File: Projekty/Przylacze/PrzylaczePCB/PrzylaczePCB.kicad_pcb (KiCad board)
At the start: 2 copper layers, 134.6 x 126 mm, 131 parts, among them J1 Conn_02x20_Odd_Even, J2 USB_B, J3 Conn_01x06, J4 Conn_02x04_Odd_Even, J5 Screw_Terminal_01x06, M3 MountingHole_3.2mm_M3, Q1 BC547, Q10 BC557, Q11 2N3904, Q12 2N7002, Q2 BC547, Q3 BC547, Q4 BC557, Q5 2N3904, Q6 BC557, Q7 BC557, Q8 BC547, Q9 BC557, SW1 SW_Push, SW2 SW_SPDT, SW3 SW_SPDT, SW4 SW_SPDT, SW5 SW_SPDT, SW6 SW_SPDT, SW7 SW_SPDT, SW8 SW_SPDT, SW9 SW_SPDT, U1 MCP2561-E-P, U2 ATSAM4S2AA-AU, U3 MCP2515-xSO, U4 TJA1055T_3_C,518, U5 MAX3485, U6 74AHC1G04, U7 LDL1117S33R, U8 DI78M05UAB, U9 74AHC1G04, Y1 20MHz

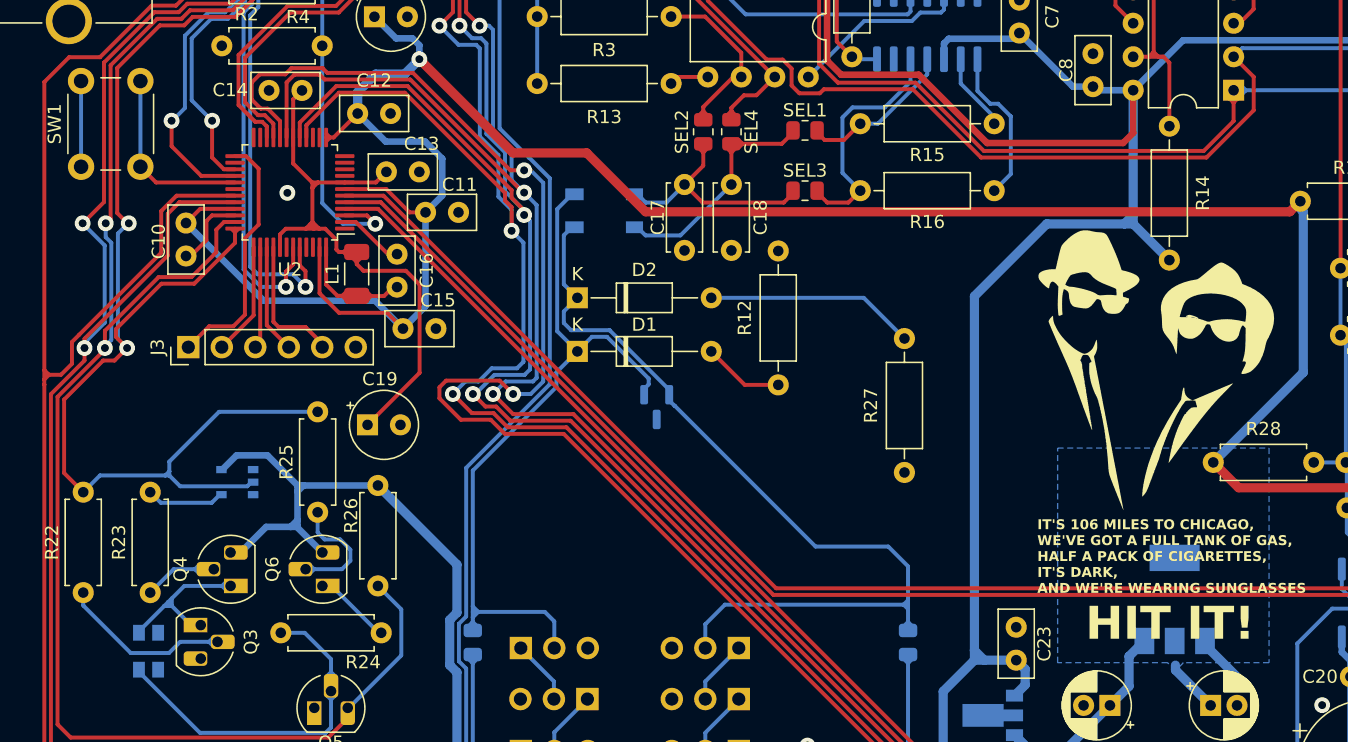
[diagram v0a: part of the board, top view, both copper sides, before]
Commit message: Przyłącze - projekt PCB v1.3.1
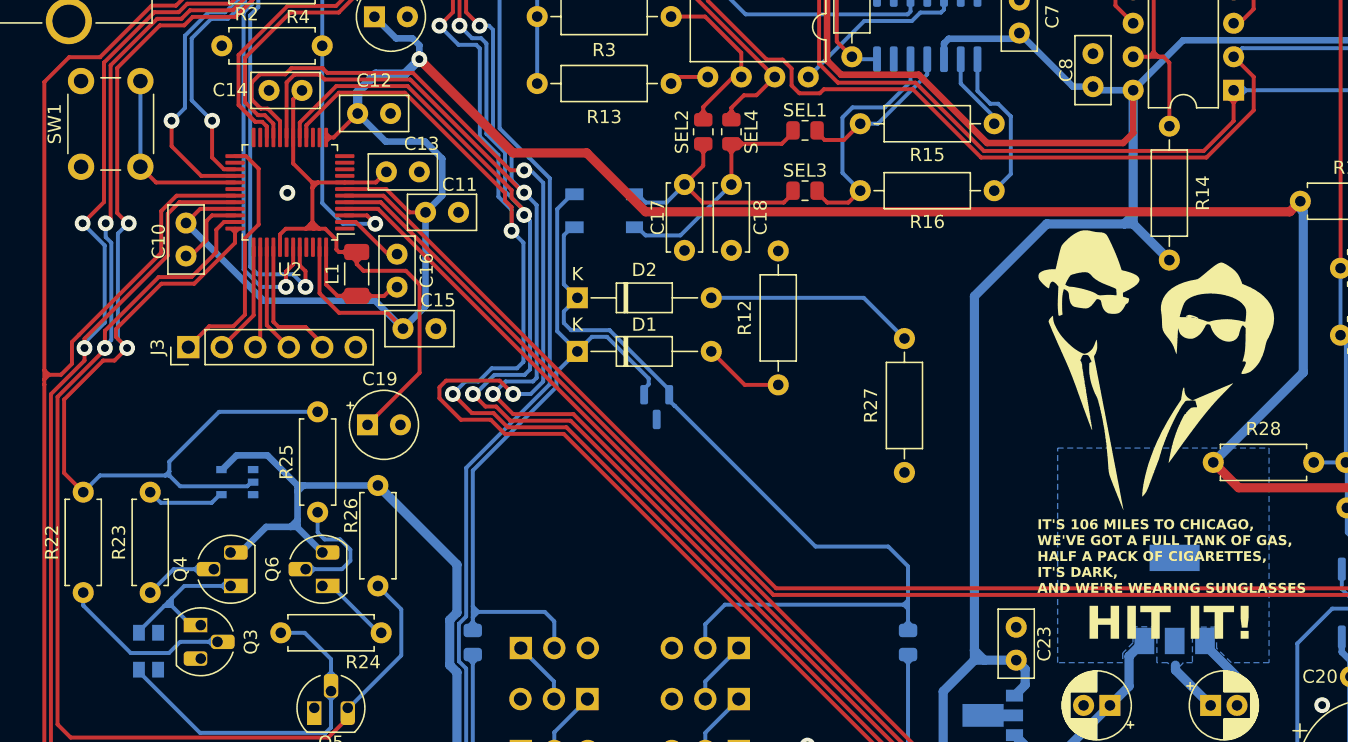
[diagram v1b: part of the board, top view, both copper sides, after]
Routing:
- net GND: track 20.7 -> 14.2 mm
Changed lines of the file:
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@@
   (via (at 102.59 166.37) (size 1.2) (drill 0.6) (layers "F.Cu" "B.Cu") (free) (net 1))
   (segment (start 132.751 158.731) (end 135.37 161.35) (width 0.7) (layer "B.Cu") (net 1))
-  (segment (start 47.49 115.96) (end 47.49 122.46) (width 0.3) (layer "B.Cu") (net 1))
   (segment (start 139.183068 125.876999) (end 139.983067 125.077) (width 0.7) (layer "F.Cu") (net 2))
   (segment (start 73.152 114.3) (end 80.264 121.412) (width 0.7) (layer "F.Cu") (net 2))
@@
         (xy 137.61 143.8)
         (xy 137.61 160.08)
+        (xy 134.75 160.08)
+        (xy 133.63 158.99)
+        (xy 133.62 157.38)
+        (xy 131.8 157.38)
+        (xy 131.8 160.08)
         (xy 131.11 160.08)
         (xy 130.51 160.7)
         (xy 129.91 160.08)
+        (xy 129.1 160.08)
+        (xy 129.1 157.36)
+        (xy 127.29 157.36)
+        (xy 127.29 158.57)
+        (xy 126.51 159.35)
+        (xy 126.51 160.08)
         (xy 121.57 160.08)
       )

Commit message: Przyłącze - projekt PCB v1.4
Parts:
- Q1, Q10, Q11, Q2, Q3, Q4, Q5, Q6, Q7, Q8, Q9: footprint Package_TO_SOT_THT:TO-92L_HandSolder -> Package_TO_SOT_THT:TO-92L
- moved C7 4.49 mm to (119.6, 114.2)
- moved R11 1.39 mm to (165.6, 93.8)
- moved C8 0.32 mm to (124.3, 114.2)
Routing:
- net Net-(Q6-B): track 9.96 -> 6.95 mm
- net +5V: track 318.7 -> 321.7 mm
- net +12V: track 106.1 -> 103.7 mm
- net Net-(Q10-B): track 9.14 -> 6.77 mm
- net Net-(D10-A): track 28.3 -> 26.1 mm
- net Net-(Q1-B): track 25.2 -> 23.1 mm
- net USBMON: track 23.8 -> 25.9 mm
- net Net-(U2-VDDPLL): track 10.0 -> 8.18 mm
- net Net-(D4-A): track 2.92 -> 4.74 mm
- net Net-(Q10-C): track 5.03 -> 6.59 mm
- net Net-(Q6-C): track 5.03 -> 6.50 mm
- net CANH: track 269.3 -> 267.9 mm
- net Net-(U2-VDDOUT): track 47.0 -> 45.8 mm
- net Net-(J2-D+): track 7.88 -> 6.81 mm
- net ERR: track 102.3 -> 103.3 mm
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- added copper zone on B.Cu, net +5V
- added copper zone on B.Cu, net Net-(U4-BAT)
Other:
- board text added: "Przyłącze stanowiskowe v1.4 Projekt kompetencyjny 2023 6EiT Grupa 7 - Sieci przemysłowe Maciej Kaczorowski, Maciej Mierzejek, Artur Poteraj, Rafał Skwirus Politechnika Łódzka WEEIA github.com/BlackHabanero/PKgr7Sieci"
- board text removed: "Przyłącze stanowiskowe v1.3 Projekt kompetencyjny 2023 6EiT Grupa 7 - Sieci przemysłowe Maciej Kaczorowski, Maciej Mierzejek, Artur Poteraj, Rafał Skwirus Politechnika Łódzka WEEIA github.com/BlackHabanero/PKgr7Sieci"

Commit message: Przyłącze - projekt PCB v1.4.1
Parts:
- J4: footprint Connector_PinHeader_2.54mm:PinHeader_2x04_P2.54mm_Vertical -> Connector_PinSocket_2.54mm:PinSocket_2x04_P2.54mm_Vertical; moved to B.Cu
- turned J4 to 180 degrees
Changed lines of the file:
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@@
     )
   )
-  (footprint "Connector_PinHeader_2.54mm:PinHeader_2x04_P2.54mm_Vertical" placed (layer "F.Cu")
-    (at 165.1 161.544)
-    (descr "Through hole straight pin header, 2x04, 2.54mm pitch, double rows")
-    (tags "Through hole pin header THT 2x04 2.54mm double row")
-    (property "Sheetfile" "PrzylaczePCB.kicad_sch")
-    (property "Sheetname" "")
-    (property "ki_description" "Generic connector, double row, 02x04, odd/even pin numbering scheme (row 1 odd numbers, row 2 even numbers), script generated (kicad-library-utils/schlib/autogen/connector/)")
-    (property "ki_keywords" "connector")
-    (attr through_hole)
-    (fp_text reference "J4" (at 1.27 -2.33) (layer "F.SilkS")
-        (effects (font (size 1 1) (thickness 0.15)))
-    )
-    (fp_text value "Conn_02x04_Odd_Even" (at 1.27 9.95) (layer "F.Fab")
-        (effects (font (size 1 1) (thickness 0.15)))
-    )
-    (fp_text user "${REFERENCE}" (at 1.27 3.81 90) (layer "F.Fab")
-        (effects (font (size 1 1) (thickness 0.15)))
-    )
-    (fp_line (start -1.33 -1.33) (end 0 -1.33)
-      (stroke (width 0.12) (type solid)) (layer "F.SilkS"))
-    (fp_line (start -1.33 0) (end -1.33 -1.33)
-      (stroke (width 0.12) (type solid)) (layer "F.SilkS"))
-    (fp_line (start -1.33 1.27) (end -1.33 8.95)
-      (stroke (width 0.12) (type solid)) (layer "F.SilkS"))
-    (fp_line (start -1.33 1.27) (end 1.27 1.27)
-      (stroke (width 0.12) (type solid)) (layer "F.SilkS"))
-    (fp_line (start -1.33 8.95) (end 3.87 8.95)
-      (stroke (width 0.12) (type solid)) (layer "F.SilkS"))
-    (fp_line (start 1.27 -1.33) (end 3.87 -1.33)
-      (stroke (width 0.12) (type solid)) (layer "F.SilkS"))
-    (fp_line (start 1.27 1.27) (end 1.27 -1.33)
-      (stroke (width 0.12) (type solid)) (layer "F.SilkS"))
-    (fp_line (start 3.87 -1.33) (end 3.87 8.95)
-      (stroke (width 0.12) (type solid)) (layer "F.SilkS"))
-    (fp_line (start -1.8 -1.8) (end -1.8 9.4)
-      (stroke (width 0.05) (type solid)) (layer "F.CrtYd"))
-    (fp_line (start -1.8 9.4) (end 4.35 9.4)
-      (stroke (width 0.05) (type solid)) (layer "F.CrtYd"))
-    (fp_line (start 4.35 -1.8) (end -1.8 -1.8)
-      (stroke (width 0.05) (type solid)) (layer "F.CrtYd"))
-    (fp_line (start 4.35 9.4) (end 4.35 -1.8)
-      (stroke (width 0.05) (type solid)) (layer "F.CrtYd"))
-    (fp_line (start -1.27 0) (end 0 -1.27)
-      (stroke (width 0.1) (type solid)) (layer "F.Fab"))
-    (fp_line (start -1.27 8.89) (end -1.27 0)
-      (stroke (width 0.1) (type solid)) (layer "F.Fab"))
-    (fp_line (start 0 -1.27) (end 3.81 -1.27)
-      (stroke (width 0.1) (type solid)) (layer "F.Fab"))
-    (fp_line (start 3.81 -1.27) (end 3.81 8.89)
-      (stroke (width 0.1) (type solid)) (layer "F.Fab"))
-    (fp_line (start 3.81 8.89) (end -1.27 8.89)
-      (stroke (width 0.1) (type solid)) (layer "F.Fab"))
-    (pad "1" thru_hole rect (at 0 0) (size 1.7 1.7) (drill 1) (layers "*.Cu" "*.Mask")
-      (net 1 "GND") (pinfunction "Pin_1") (pintype "passive"))
-    (pad "2" thru_hole oval (at 2.54 0) (size 1.7 1.7) (drill 1) (layers "*.Cu" "*.Mask")
-      (net 2 "+3.3V") (pinfunction "Pin_2") (pintype "passive"))
-    (pad "3" thru_hole oval (at 0 2.54) (size 1.7 1.7) (drill 1) (layers "*.Cu" "*.Mask")
-      (net 31 "CS0") (pinfunction "Pin_3") (pintype "passive"))
-    (pad "4" thru_hole oval (at 2.54 2.54) (size 1.7 1.7) (drill 1) (layers "*.Cu" "*.Mask")
-      (net 2 "+3.3V") (pinfunction "Pin_4") (pintype "passive"))
-    (pad "5" thru_hole oval (at 0 5.08) (size 1.7 1.7) (drill 1) (layers "*.Cu" "*.Mask")
-      (net 32 "SPCK") (pinfunction "Pin_5") (pintype "passive"))
-    (pad "6" thru_hole oval (at 2.54 5.08) (size 1.7 1.7) (drill 1) (layers "*.Cu" "*.Mask")
-      (net 33 "MOSI") (pinfunction "Pin_6") (pintype "passive"))
-    (pad "7" thru_hole oval (at 0 7.62) (size 1.7 1.7) (drill 1) (layers "*.Cu" "*.Mask")
-      (net 34 "MISO") (pinfunction "Pin_7") (pintype "passive"))
-    (pad "8" thru_hole oval (at 2.54 7.62) (size 1.7 1.7) (drill 1) (layers "*.Cu" "*.Mask")
-      (net 35 "RADIO_IRQ") (pinfunction "Pin_8") (pintype "passive"))
-    (model "${KICAD6_3DMODEL_DIR}/Connector_PinHeader_2.54mm.3dshapes/PinHeader_2x04_P2.54mm_Vertical.wrl"
-      (offset (xyz 0 0 0))
-      (scale (xyz 1 1 1))
-      (rotate (xyz 0 0 0))
-    )
-  )
   (footprint "Resistor_THT:R_Axial_DIN0207_L6.3mm_D2.5mm_P10.16mm_Horizontal" placed (layer "F.Cu")
     (at 105.966 103.955 -90)
@@
       (rotate (xyz 0 0 0))
     )
+    (model "${KIPRJMOD}/3DModels/USB-B-S-F-B-TH.stp"
+      (offset (xyz 7 -1.25 0))
+      (scale (xyz 1 1 1))
+      (rotate (xyz 90 180 90))
+    )
   )
   (footprint "Resistor_THT:R_Axial_DIN0207_L6.3mm_D2.5mm_P7.62mm_Horizontal" placed (layer "F.Cu")
@@
     (pad "6" thru_hole circle (at 25.4 0) (size 3 3) (drill 1.5) (layers "*.Cu" "*.Mask")
       (net 1 "GND") (pinfunction "Pin_6") (pintype "passive"))
-    (model "${KICAD6_3DMODEL_DIR}/TerminalBlock.3dshapes/TerminalBlock_bornier-6_P5.08mm.wrl"
+    (model "${KIPRJMOD}/3DModels/TerminalBlock_bornier-6_P5.08mm.wrl"
       (offset (xyz 12.69999981 0 0))
       (scale (xyz 1 1 1))
@@
     )
   )
+  (footprint "Connector_PinSocket_2.54mm:PinSocket_2x04_P2.54mm_Vertical" (layer "B.Cu")
+    (at 165.1 161.544 180)
+    (descr "Through hole straight socket strip, 2x04, 2.54mm pitch, double cols (from Kicad 4.0.7), script generated")
+    (tags "Through hole socket strip THT 2x04 2.54mm double row")
+    (property "Sheetfile" "PrzylaczePCB.kicad_sch")
+    (property "Sheetname" "")
+    (property "ki_description" "Generic connector, double row, 02x04, odd/even pin numbering scheme (row 1 odd numbers, row 2 even numbers), script generated (kicad-library-utils/schlib/autogen/connector/)")
+    (property "ki_keywords" "connector")
+    (attr through_hole)
+    (fp_text reference "J4" (at -1.27 2.77) (layer "B.SilkS")
+        (effects (font (size 1 1) (thickness 0.15)) (justify mirror))
+    )
+    (fp_text value "Conn_02x04_Odd_Even" (at -1.27 -10.39) (layer "B.Fab")
+        (effects (font (size 1 1) (thickness 0.15)) (justify mirror))
+    )
+    (fp_text user "${REFERENCE}" (at -1.27 -3.81 90) (layer "B.Fab")
+        (effects (font (size 1 1) (thickness 0.15)) (justify mirror))
+    )
+    (fp_line (start -3.87 -8.95) (end 1.33 -8.95)
+      (stroke (width 0.12) (type solid)) (layer "B.SilkS"))
+    (fp_line (start -3.87 1.33) (end -3.87 -8.95)
+      (stroke (width 0.12) (type solid)) (layer "B.SilkS"))
+    (fp_line (start -3.87 1.33) (end -1.27 1.33)
+      (stroke (width 0.12) (type solid)) (layer "B.SilkS"))
+    (fp_line (start -1.27 -1.27) (end 1.33 -1.27)
+      (stroke (width 0.12) (type solid)) (layer "B.SilkS"))
+    (fp_line (start -1.27 1.33) (end -1.27 -1.27)
+      (stroke (width 0.12) (type solid)) (layer "B.SilkS"))
+    (fp_line (start 0 1.33) (end 1.33 1.33)
+      (stroke (width 0.12) (type solid)) (layer "B.SilkS"))
+    (fp_line (start 1.33 -1.27) (end 1.33 -8.95)
+      (stroke (width 0.12) (type solid)) (layer "B.SilkS"))
+    (fp_line (start 1.33 1.33) (end 1.33 0)
+      (stroke (width 0.12) (type solid)) (layer "B.SilkS"))
+    (fp_line (start -4.34 -9.4) (end -4.34 1.8)
+      (stroke (width 0.05) (type solid)) (layer "B.CrtYd"))
+    (fp_line (start -4.34 1.8) (end 1.76 1.8)
+      (stroke (width 0.05) (type solid)) (layer "B.CrtYd"))
+    (fp_line (start 1.76 -9.4) (end -4.34 -9.4)
+      (stroke (width 0.05) (type solid)) (layer "B.CrtYd"))
+    (fp_line (start 1.76 1.8) (end 1.76 -9.4)
+      (stroke (width 0.05) (type solid)) (layer "B.CrtYd"))
+    (fp_line (start -3.81 -8.89) (end -3.81 1.27)
+      (stroke (width 0.1) (type solid)) (layer "B.Fab"))
+    (fp_line (start -3.81 1.27) (end 0.27 1.27)
+      (stroke (width 0.1) (type solid)) (layer "B.Fab"))
+    (fp_line (start 0.27 1.27) (end 1.27 0.27)
+      (stroke (width 0.1) (type solid)) (layer "B.Fab"))
+    (fp_line (start 1.27 -8.89) (end -3.81 -8.89)
+      (stroke (width 0.1) (type solid)) (layer "B.Fab"))
+    (fp_line (start 1.27 0.27) (end 1.27 -8.89)
+      (stroke (width 0.1) (type solid)) (layer "B.Fab"))
+    (pad "1" thru_hole rect (at 0 0 180) (size 1.7 1.7) (drill 1) (layers "*.Cu" "*.Mask")
+      (net 1 "GND") (pinfunction "Pin_1") (pintype "passive"))
+    (pad "2" thru_hole oval (at -2.54 0 180) (size 1.7 1.7) (drill 1) (layers "*.Cu" "*.Mask")
+      (net 2 "+3.3V") (pinfunction "Pin_2") (pintype "passive"))
+    (pad "3" thru_hole oval (at 0 -2.54 180) (size 1.7 1.7) (drill 1) (layers "*.Cu" "*.Mask")
+      (net 31 "CS0") (pinfunction "Pin_3") (pintype "passive"))
+    (pad "4" thru_hole oval (at -2.54 -2.54 180) (size 1.7 1.7) (drill 1) (layers "*.Cu" "*.Mask")
+      (net 2 "+3.3V") (pinfunction "Pin_4") (pintype "passive"))
+    (pad "5" thru_hole oval (at 0 -5.08 180) (size 1.7 1.7) (drill 1) (layers "*.Cu" "*.Mask")
+      (net 32 "SPCK") (pinfunction "Pin_5") (pintype "passive"))
+    (pad "6" thru_hole oval (at -2.54 -5.08 180) (size 1.7 1.7) (drill 1) (layers "*.Cu" "*.Mask")
+      (net 33 "MOSI") (pinfunction "Pin_6") (pintype "passive"))
+    (pad "7" thru_hole oval (at 0 -7.62 180) (size 1.7 1.7) (drill 1) (layers "*.Cu" "*.Mask")
+      (net 34 "MISO") (pinfunction "Pin_7") (pintype "passive"))
+    (pad "8" thru_hole oval (at -2.54 -7.62 180) (size 1.7 1.7) (drill 1) (layers "*.Cu" "*.Mask")
+      (net 35 "RADIO_IRQ") (pinfunction "Pin_8") (pintype "passive"))
+    (model "${KICAD6_3DMODEL_DIR}/Connector_PinSocket_2.54mm.3dshapes/PinSocket_2x04_P2.54mm_Vertical.wrl"
+      (offset (xyz 0 0 0))
+      (scale (xyz 1 1 1))
+      (rotate (xyz 0 0 0))
+    )
+  )
   (footprint "PrzylaczeFootprintLibrary:Nexperia-SOT753-10_2018-0-0" placed (layer "B.Cu")
     (at 59.3395 146.3845 -90)
@@
         (xy 118.91 162.15)
         (xy 118.69 161.58)
-        (xy 118.19 161.58)
       )
     )
